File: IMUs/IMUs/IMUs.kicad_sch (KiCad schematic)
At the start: 3 parts, among them U1 LSM6DSO32TR

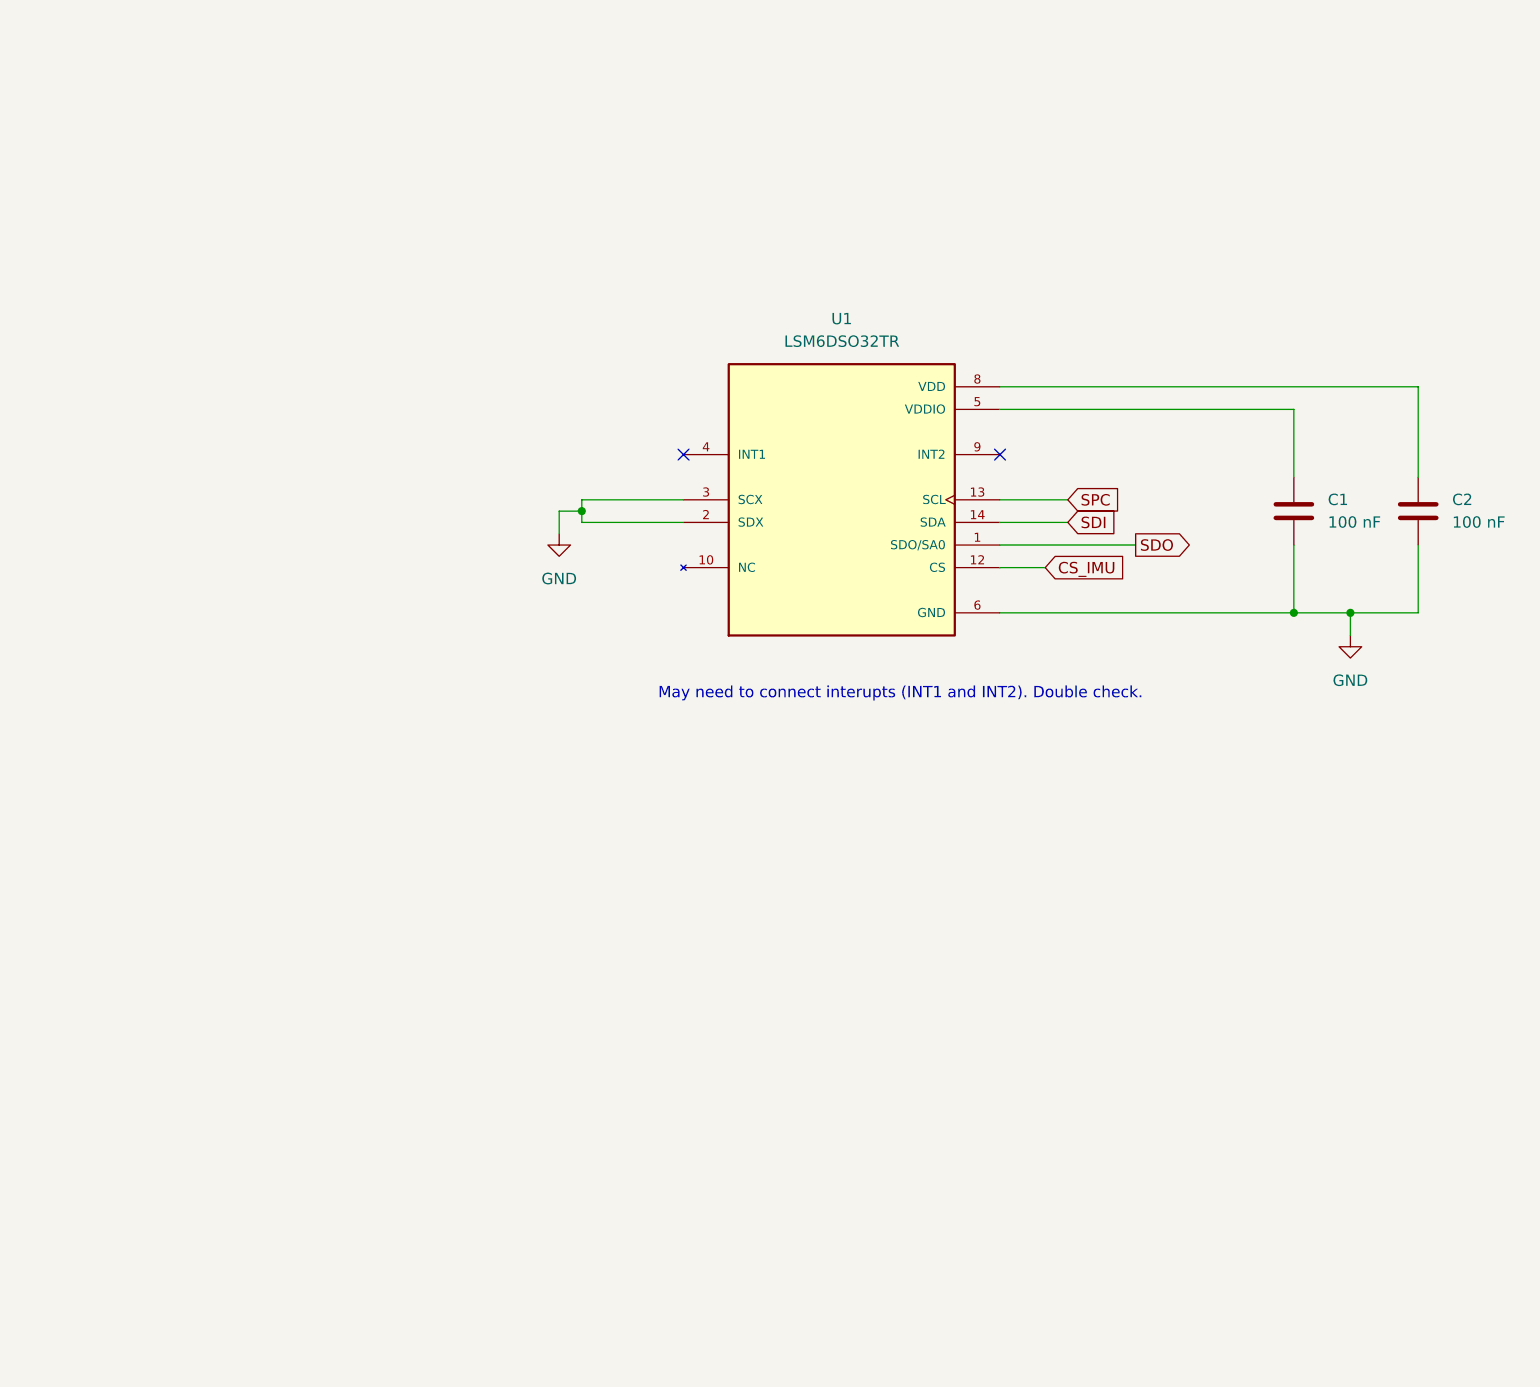
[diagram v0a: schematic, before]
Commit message: Added second IMU schematic.
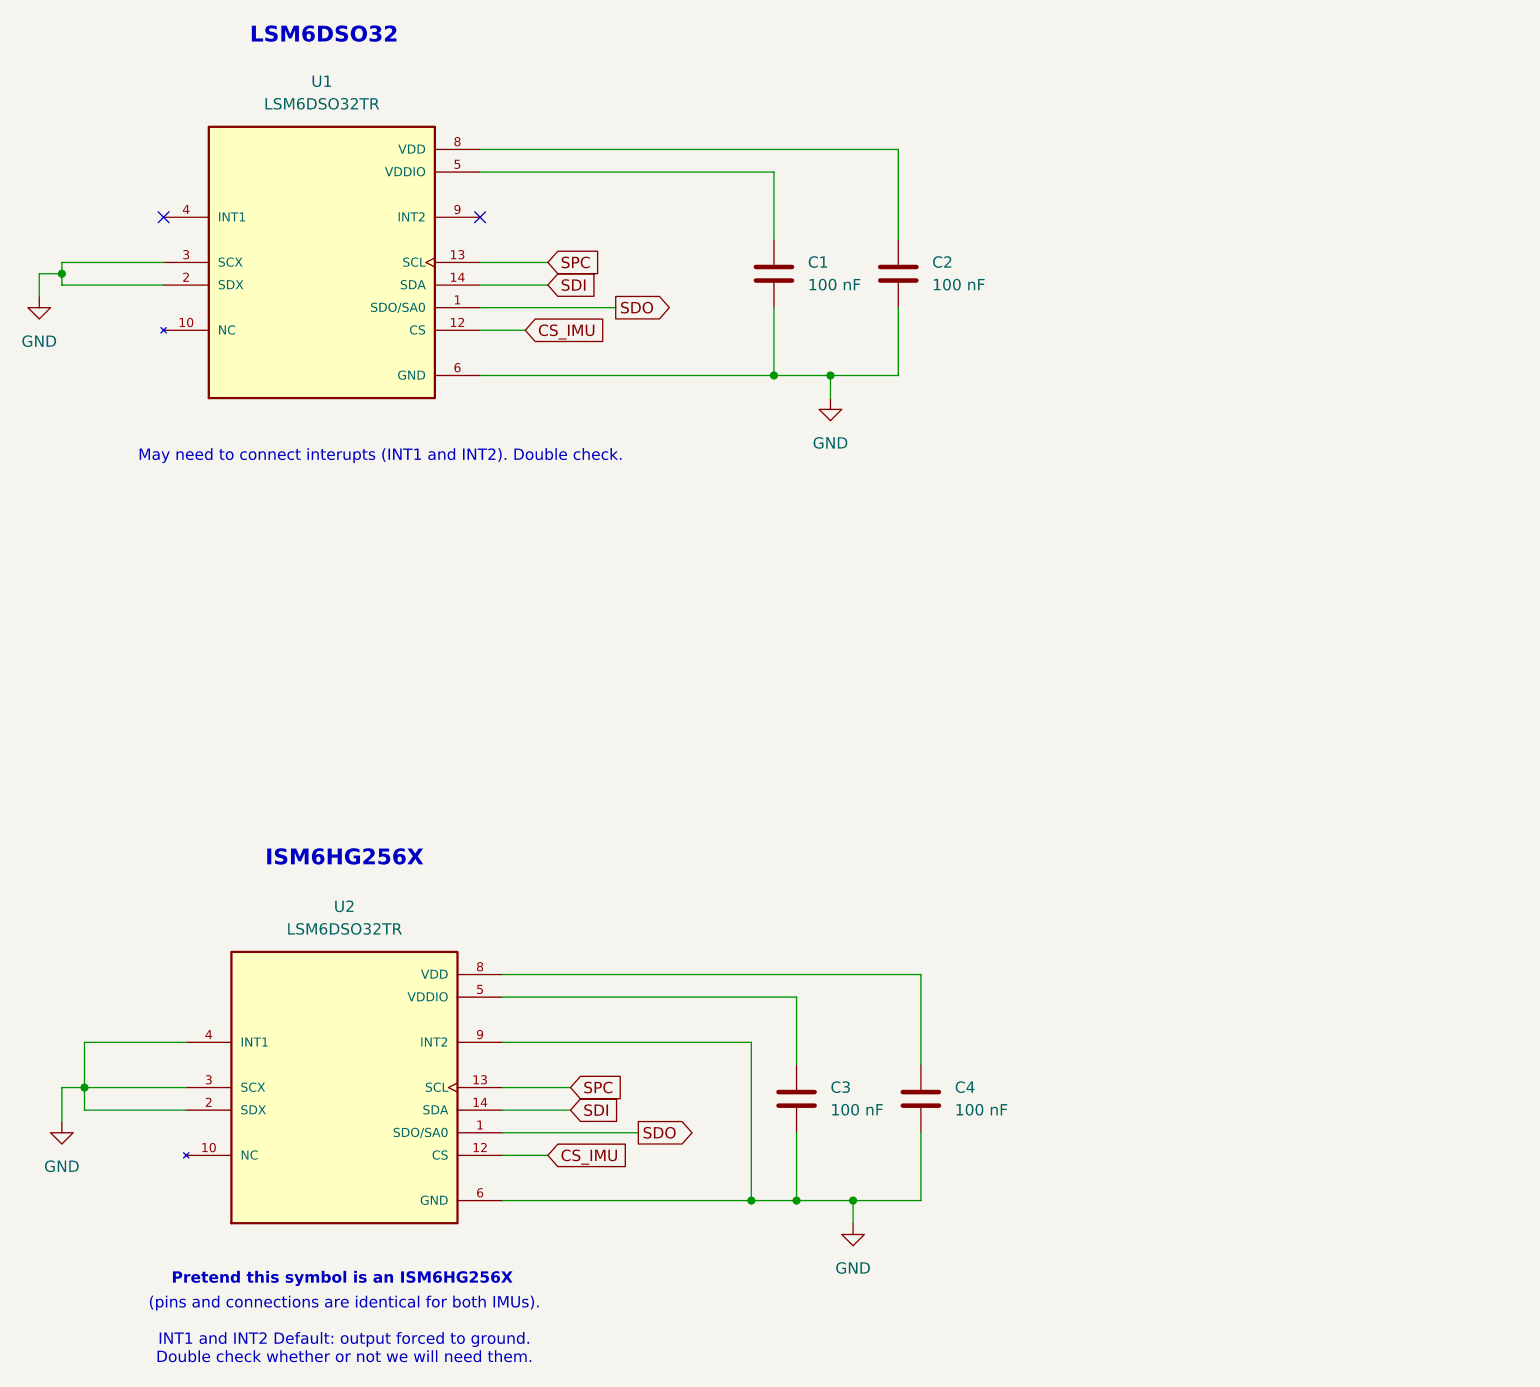
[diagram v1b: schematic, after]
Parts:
- added C3, C4: 100 nF, symbol Device:C
- added U2: LSM6DSO32TR, LSM6DSO32TR:XDCR_LSM6DSO32TR, symbol LSM6DSO32:LSM6DSO32TR
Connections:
- net CS_IMU: now also U2.12 (CS)
- net GND: now also C3.2, C4.2, U2.2 (SDX), U2.3 (SCX), U2.4 (INT1), U2.6 (GND), U2.7 (GND), U2.9 (INT2)
- net SDI: now also U2.14 (SDA)
- net SDO: now also U2.1 (SDO/SA0)
- net SPC: now also U2.13 (SCL)
- new net: U2.10 (NC), U2.11 (NC)
- new net: C3.1, U2.5 (VDDIO)
- new net: C4.1, U2.8 (VDD)
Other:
- note added: "(pins and connections are identical for both IMUs). INT1 and INT2 Default: output forced to ground. Double check whether or not we will need them."
- note added: "ISM6HG256X"
- note added: "LSM6DSO32"
- note added: "Pretend this symbol is an ISM6HG256X"
- moved on the sheet: C1, C2, U1
